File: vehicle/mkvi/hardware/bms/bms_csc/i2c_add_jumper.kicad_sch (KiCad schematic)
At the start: 4 parts

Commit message: Replace all mentions of Peripheral with CSC
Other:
- title: Peripheral | I2C Address Jumper -> MkVI BMS Cell Supervisory Circuit
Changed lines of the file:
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@@
   (paper "A")
   (title_block
-    (title "Peripheral | I2C Address Jumper")
+    (title "MkVI BMS Cell Supervisory Circuit")
     (date "2022-12-04")
     (rev "0")

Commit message: Finalize boards for fab (#217)
* add BOM tool to join BOMs

* add custom BOM script for working with custom BOM fields

* add patched QR plugin for better QR codes

* add logo and authors to boards

* update parts library and fix misc issues

* migrate projects to new parts library
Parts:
- JP19, JP20: now left out of the parts list
- R51, R52: symbol formula:R_4.99K -> OEM:4K99R; DKPN (none) -> RMCF0603FT4K99DKR-ND; MFN DK -> Stackpole Electronics; MPN RNCP0805FTD4K99CT-ND -> RMCF0603FT4K99; NewDesigns (none) -> YES; Package (none) -> 0603; PurchasingLink https://www.digikey.com/product-detail/en/stackpole-electro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 -> (none); Stocked (none) -> Digi-Reel; Style (none) -> SMD
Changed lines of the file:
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@@
   )
   (symbol (lib_id "Jumper:SolderJumper_3_Open") (at 144.78 88.9 270) (unit 1)
-    (in_bom yes) (on_board yes) (fields_autoplaced)
+    (in_bom no) (on_board yes) (fields_autoplaced)
     (property "Reference" "JP19" (id 0) (at 147.32 87.6299 90)
       (effects (font (size 1.27 1.27)) (justify left))
@@
     (pin "3")
   )
-  (symbol (lib_id "formula:R_4.99K") (at 184.15 81.28 0) (unit 1)
+  (symbol (lib_id "OEM:4K99R") (at 184.15 81.28 0) (unit 1)
     (in_bom yes) (on_board yes)
     (property "Reference" "R51" (id 0) (at 179.07 85.09 90)
@@
       (effects (font (size 1.27 1.27)) hide)
     )
-    (property "Datasheet" "https://www.susumu.co.jp/common/pdf/n_catalog_partition01_en.pdf" (id 3) (at 181.61 80.01 0)
+    (property "Datasheet" "https://www.seielect.com/Catalog/SEI-RMCF_RMCP.pdf" (id 3) (at 181.61 80.01 0)
       (effects (font (size 1.27 1.27)) hide)
     )
-    (property "MPN" "RNCP0805FTD4K99CT-ND" (id 4) (at 185.928 81.28 0)
+    (property "MPN" "RMCF0603FT4K99" (id 4) (at 185.928 81.28 0)
       (effects (font (size 1.27 1.27)) (justify left) hide)
     )
-    (property "MFN" "DK" (id 5) (at 185.928 83.5914 0)
+    (property "MFN" "Stackpole Electronics" (id 5) (at 185.928 83.5914 0)
       (effects (font (size 1.27 1.27)) (justify left) hide)
     )
-    (property "PurchasingLink" "https://www.digikey.com/product-detail/en/stackpole-electronics-inc/RNCP0805FTD4K99/RNCP0805FTD4K99CT-ND/2240591" (id 6) (at 185.928 85.9028 0)
-      (effects (font (size 1.27 1.27)) (justify left) hide)
+    (property "DKPN" "RMCF0603FT4K99DKR-ND" (id 6) (at 184.15 81.28 0)
+      (effects (font (size 1.27 1.27)) hide)
+    )
+    (property "NewDesigns" "YES" (id 7) (at 184.15 81.28 0)
+      (effects (font (size 1.27 1.27)) hide)
+    )
+    (property "Stocked" "Digi-Reel" (id 8) (at 184.15 81.28 0)
+      (effects (font (size 1.27 1.27)) hide)
+    )
+    (property "Package" "0603" (id 9) (at 184.15 81.28 0)
+      (effects (font (size 1.27 1.27)) hide)
+    )
+    (property "Style" "SMD" (id 10) (at 184.15 81.28 0)
+      (effects (font (size 1.27 1.27)) hide)
     )
     (pin "1")
@@
   )
   (symbol (lib_id "Jumper:SolderJumper_3_Open") (at 144.78 110.49 270) (unit 1)
-    (in_bom yes) (on_board yes) (fields_autoplaced)
+    (in_bom no) (on_board yes) (fields_autoplaced)
     (property "Reference" "JP20" (id 0) (at 147.32 109.2199 90)
       (effects (font (size 1.27 1.27)) (justify left))
@@
     (pin "3")
   )
-  (symbol (lib_id "formula:R_4.99K") (at 184.15 118.11 0) (unit 1)
+  (symbol (lib_id "OEM:4K99R") (at 184.15 118.11 0) (unit 1)
     (in_bom yes) (on_board yes)
     (property "Reference" "R52" (id 0) (at 179.07 121.92 90)
@@
       (effects (font (size 1.27 1.27)) hide)
     )
-    (property "Datasheet" "https://www.susumu.co.jp/common/pdf/n_catalog_partition01_en.pdf" (id 3) (at 181.61 116.84 0)
+    (property "Datasheet" "https://www.seielect.com/Catalog/SEI-RMCF_RMCP.pdf" (id 3) (at 181.61 116.84 0)
       (effects (font (size 1.27 1.27)) hide)
     )
-    (property "MPN" "RNCP0805FTD4K99CT-ND" (id 4) (at 185.928 118.11 0)
+    (property "MPN" "RMCF0603FT4K99" (id 4) (at 185.928 118.11 0)
       (effects (font (size 1.27 1.27)) (justify left) hide)
     )
-    (property "MFN" "DK" (id 5) (at 185.928 120.4214 0)
+    (property "MFN" "Stackpole Electronics" (id 5) (at 185.928 120.4214 0)
       (effects (font (size 1.27 1.27)) (justify left) hide)
     )
-    (property "PurchasingLink" "https://www.digikey.com/product-detail/en/stackpole-electronics-inc/RNCP0805FTD4K99/RNCP0805FTD4K99CT-ND/2240591" (id 6) (at 185.928 122.7328 0)
-      (effects (font (size 1.27 1.27)) (justify left) hide)
+    (property "DKPN" "RMCF0603FT4K99DKR-ND" (id 6) (at 184.15 118.11 0)
+      (effects (font (size 1.27 1.27)) hide)
+    )
+    (property "NewDesigns" "YES" (id 7) (at 184.15 118.11 0)
+      (effects (font (size 1.27 1.27)) hide)
+    )
+    (property "Stocked" "Digi-Reel" (id 8) (at 184.15 118.11 0)
+      (effects (font (size 1.27 1.27)) hide)
+    )
+    (property "Package" "0603" (id 9) (at 184.15 118.11 0)
+      (effects (font (size 1.27 1.27)) hide)
+    )
+    (property "Style" "SMD" (id 10) (at 184.15 118.11 0)
+      (effects (font (size 1.27 1.27)) hide)
     )
     (pin "1")

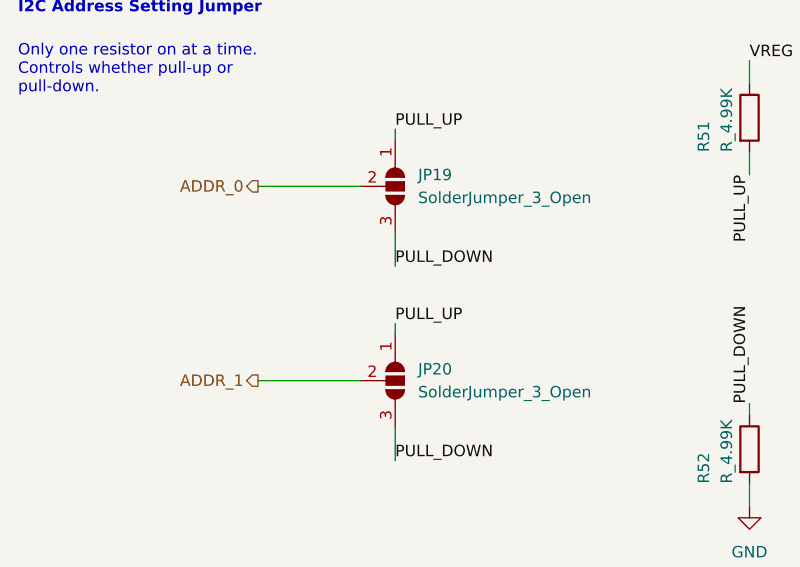
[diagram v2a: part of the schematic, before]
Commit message: Migrate All Projects to Kicad 7
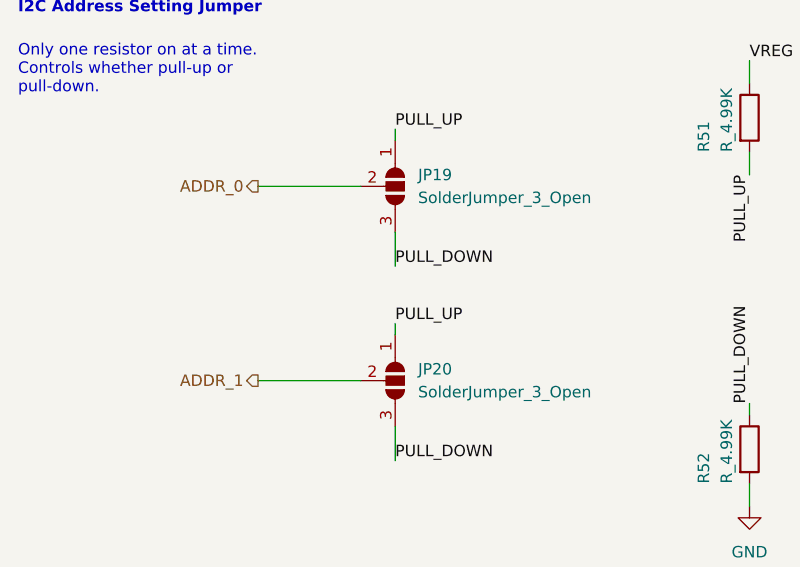
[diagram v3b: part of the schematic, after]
